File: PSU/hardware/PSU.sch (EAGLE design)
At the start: 202 parts, among them J1 SWD, J2 UART, Q1 PMOS-DPAK, Q10 PMOS-SOT23, Q11 NPN, Q2 PMOS-SOT23, Q3 NPN, Q4 PMOS-SOT23, Q5 NMOS-SOT23, Q6 PMOS-DPAK, Q7 PMOS-SOT23, Q8 NMOS-SOT23, Q9 PMOS-DPAK, U1 LM2576, U10 4069, U11 LTV-247, U12 74HC08, U13 STM8S003K3T6C, U14 74HC08, U15 4051, U16 358, U17 358, U18 74HC32, U2 MT3608, U3 7805, U4 324, U5 MC34063, U6 MT3608, U7 LM2576, U8 MC34063, U9 TP4056

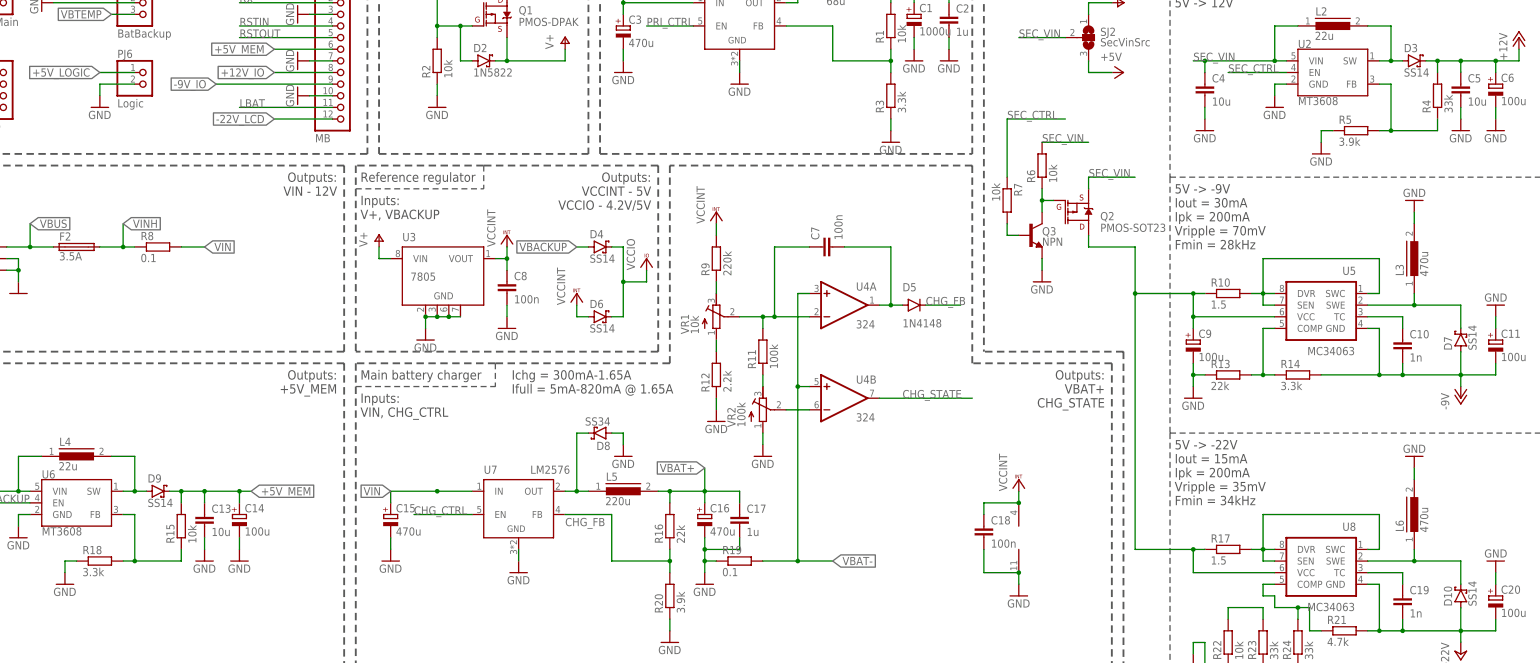
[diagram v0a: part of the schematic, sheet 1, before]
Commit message: [HW/PSU] Fix MT3608 feedback divider values
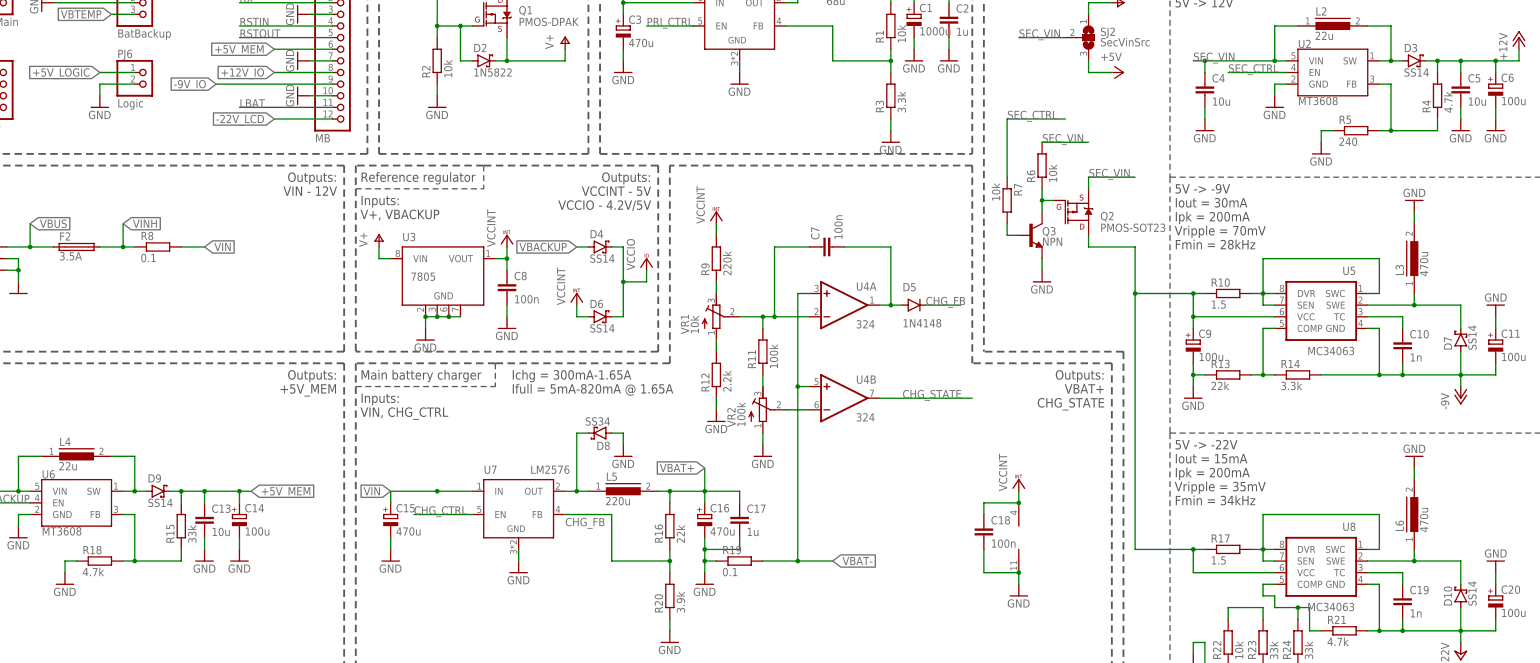
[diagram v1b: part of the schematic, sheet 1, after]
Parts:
- R15: value 10k -> 33k
- R18: value 3.3k -> 4.7k
- R4: value 33k -> 4.7k
- R5: value 3.9k -> 240
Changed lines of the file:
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@@
 </part>
 <part name="L3" library="custom" deviceset="COIL0608" device="" value="470u"/>
-<part name="R4" library="rcl" library_urn="urn:adsk.eagle:library:334" deviceset="R-EU_" device="R0805" package3d_urn="urn:adsk.eagle:package:23553/2" value="33k"/>
+<part name="R4" library="rcl" library_urn="urn:adsk.eagle:library:334" deviceset="R-EU_" device="R0805" package3d_urn="urn:adsk.eagle:package:23553/2" value="4.7k"/>
 <part name="C4" library="rcl" library_urn="urn:adsk.eagle:library:334" deviceset="C-EU" device="C1206" package3d_urn="urn:adsk.eagle:package:23618/2" value="10u"/>
 <part name="GND34" library="supply1" library_urn="urn:adsk.eagle:library:371" deviceset="GND" device=""/>
@@
 <part name="C5" library="rcl" library_urn="urn:adsk.eagle:library:334" deviceset="C-EU" device="C1206" package3d_urn="urn:adsk.eagle:package:23618/2" value="10u"/>
 <part name="GND36" library="supply1" library_urn="urn:adsk.eagle:library:371" deviceset="GND" device=""/>
-<part name="R5" library="rcl" library_urn="urn:adsk.eagle:library:334" deviceset="R-EU_" device="R0805" package3d_urn="urn:adsk.eagle:package:23553/2" value="3.9k"/>
+<part name="R5" library="rcl" library_urn="urn:adsk.eagle:library:334" deviceset="R-EU_" device="R0805" package3d_urn="urn:adsk.eagle:package:23553/2" value="240"/>
 <part name="GND37" library="supply1" library_urn="urn:adsk.eagle:library:371" deviceset="GND" device=""/>
 <part name="C6" library="rcl" library_urn="urn:adsk.eagle:library:334" deviceset="CPOL-EU" device="E3.5-8" package3d_urn="urn:adsk.eagle:package:23360/2" value="100u"/>
@@
 <part name="GND56" library="supply1" library_urn="urn:adsk.eagle:library:371" deviceset="GND" device=""/>
 <part name="U6" library="custom" deviceset="MT3608" device="" value="MT3608"/>
-<part name="R15" library="rcl" library_urn="urn:adsk.eagle:library:334" deviceset="R-EU_" device="R0805" package3d_urn="urn:adsk.eagle:package:23553/2" value="10k"/>
+<part name="R15" library="rcl" library_urn="urn:adsk.eagle:library:334" deviceset="R-EU_" device="R0805" package3d_urn="urn:adsk.eagle:package:23553/2" value="33k"/>
 <part name="C12" library="rcl" library_urn="urn:adsk.eagle:library:334" deviceset="C-EU" device="C1206" package3d_urn="urn:adsk.eagle:package:23618/2" value="10u"/>
 <part name="GND57" library="supply1" library_urn="urn:adsk.eagle:library:371" deviceset="GND" device=""/>
@@
 <part name="C13" library="rcl" library_urn="urn:adsk.eagle:library:334" deviceset="C-EU" device="C1206" package3d_urn="urn:adsk.eagle:package:23618/2" value="10u"/>
 <part name="GND59" library="supply1" library_urn="urn:adsk.eagle:library:371" deviceset="GND" device=""/>
-<part name="R18" library="rcl" library_urn="urn:adsk.eagle:library:334" deviceset="R-EU_" device="R0805" package3d_urn="urn:adsk.eagle:package:23553/2" value="3.3k"/>
+<part name="R18" library="rcl" library_urn="urn:adsk.eagle:library:334" deviceset="R-EU_" device="R0805" package3d_urn="urn:adsk.eagle:package:23553/2" value="4.7k"/>
 <part name="GND60" library="supply1" library_urn="urn:adsk.eagle:library:371" deviceset="GND" device=""/>
 <part name="C14" library="rcl" library_urn="urn:adsk.eagle:library:334" deviceset="CPOL-EU" device="E3.5-8" package3d_urn="urn:adsk.eagle:package:23360/2" value="100u"/>

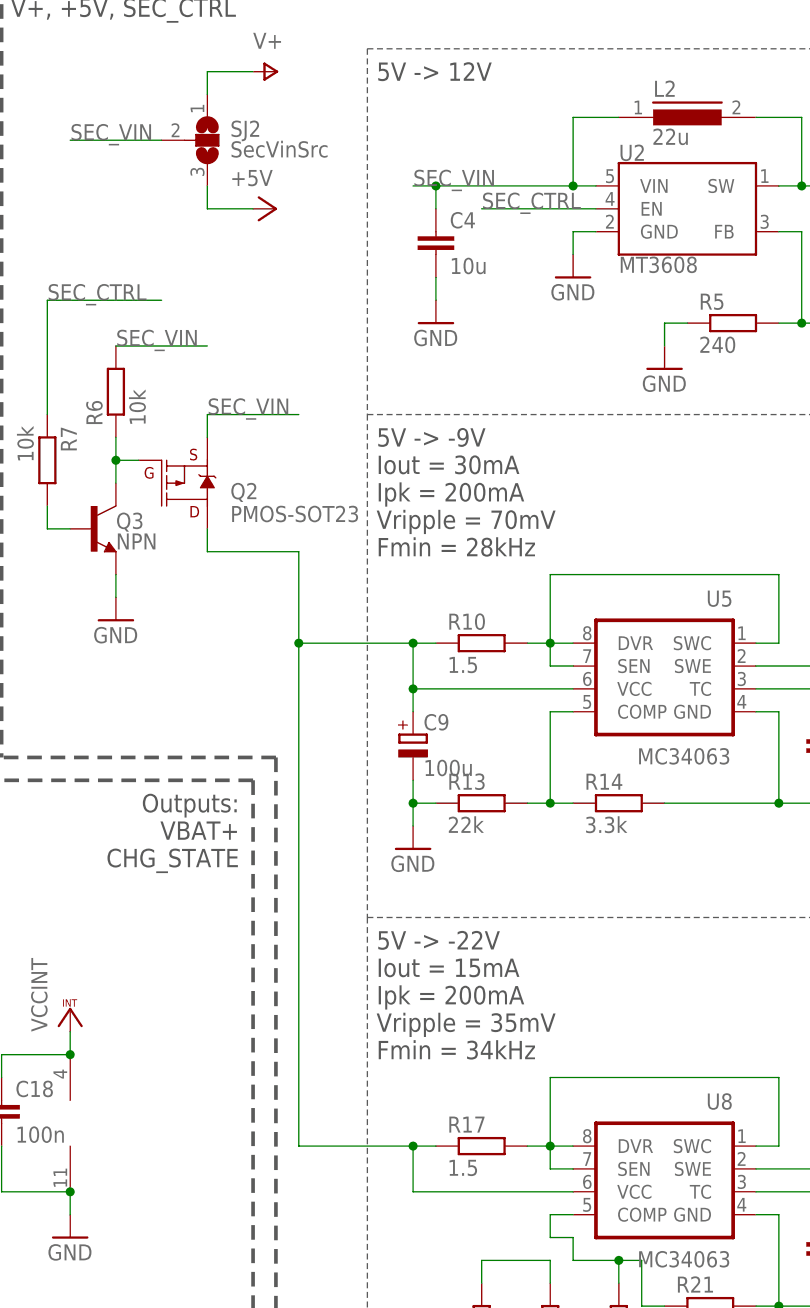
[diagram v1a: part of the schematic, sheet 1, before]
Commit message: [HW/PSU] Fix secondary 12V regulator enabling
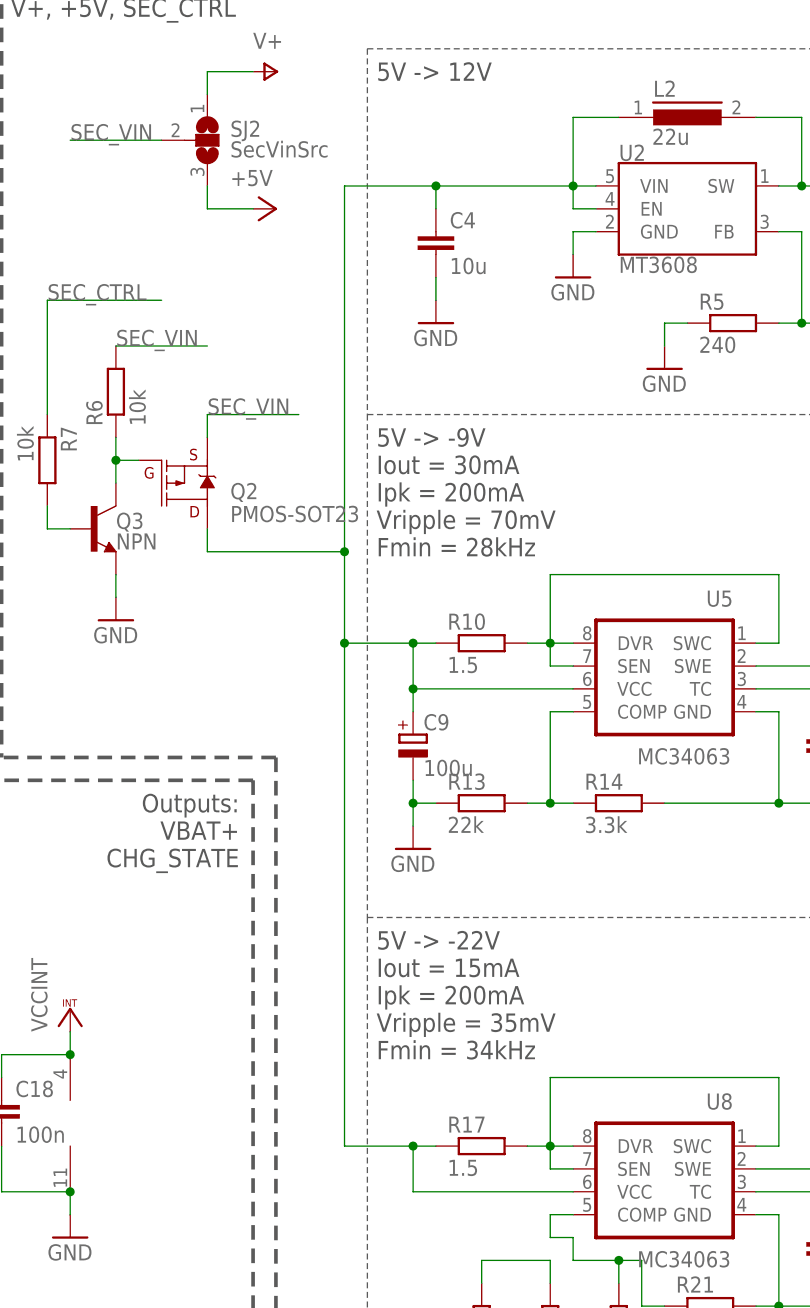
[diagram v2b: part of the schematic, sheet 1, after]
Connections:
- net SEC_CTRL: no longer U2.EN
- net SEC_VIN: no longer C4.1, L2.1, U2.VIN
- net SEC_VIN_SW: now also C4.1, L2.1, U2.EN, U2.VIN
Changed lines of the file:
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@@
-</segment>
-<segment>
-<pinref part="U2" gate="G$1" pin="VIN"/>
-<wire x1="325.12" y1="220.98" x2="322.58" y2="220.98" width="0.1524" layer="91"/>
-<pinref part="C4" gate="G$1" pin="1"/>
-<wire x1="322.58" y1="220.98" x2="307.34" y2="220.98" width="0.1524" layer="91"/>
-<wire x1="307.34" y1="220.98" x2="307.34" y2="218.44" width="0.1524" layer="91"/>
-<wire x1="327.66" y1="228.6" x2="322.58" y2="228.6" width="0.1524" layer="91"/>
-<wire x1="322.58" y1="228.6" x2="322.58" y2="220.98" width="0.1524" layer="91"/>
-<junction x="322.58" y="220.98"/>
-<wire x1="307.34" y1="220.98" x2="304.8" y2="220.98" width="0.1524" layer="91"/>
-<junction x="307.34" y="220.98"/>
-<label x="304.8" y="220.98" size="1.778" layer="95"/>
-<pinref part="L2" gate="G$1" pin="1"/>
 </segment>
 <segment>
@@
 </net>
 <net name="SEC_CTRL" class="1">
-<segment>
-<pinref part="U2" gate="G$1" pin="EN"/>
-<wire x1="325.12" y1="218.44" x2="312.42" y2="218.44" width="0.1524" layer="91"/>
-<label x="312.42" y="218.44" size="1.778" layer="95"/>
-</segment>
 <segment>
 <pinref part="R7" gate="G$1" pin="1"/>
@@
 <segment>
 <pinref part="U8" gate="G$1" pin="VCC"/>
-<wire x1="292.1" y1="180.34" x2="292.1" y2="170.18" width="0.1524" layer="91"/>
-<wire x1="292.1" y1="170.18" x2="292.1" y2="114.3" width="0.1524" layer="91"/>
+<wire x1="297.18" y1="180.34" x2="297.18" y2="170.18" width="0.1524" layer="91"/>
+<wire x1="297.18" y1="170.18" x2="297.18" y2="114.3" width="0.1524" layer="91"/>
 <wire x1="322.58" y1="109.22" x2="304.8" y2="109.22" width="0.1524" layer="91"/>
 <wire x1="304.8" y1="109.22" x2="304.8" y2="114.3" width="0.1524" layer="91"/>
 <pinref part="R17" gate="G$1" pin="1"/>
 <wire x1="307.34" y1="114.3" x2="304.8" y2="114.3" width="0.1524" layer="91"/>
-<wire x1="292.1" y1="114.3" x2="304.8" y2="114.3" width="0.1524" layer="91"/>
+<wire x1="297.18" y1="114.3" x2="304.8" y2="114.3" width="0.1524" layer="91"/>
 <junction x="304.8" y="114.3"/>
 <pinref part="Q2" gate="G$1" pin="D"/>
 <wire x1="281.94" y1="182.88" x2="281.94" y2="180.34" width="0.1524" layer="91"/>
-<wire x1="281.94" y1="180.34" x2="292.1" y2="180.34" width="0.1524" layer="91"/>
+<wire x1="281.94" y1="180.34" x2="297.18" y2="180.34" width="0.1524" layer="91"/>
 <pinref part="C9" gate="G$1" pin="+"/>
 <pinref part="R10" gate="G$1" pin="1"/>
@@
 <junction x="304.8" y="165.1"/>
 <wire x1="304.8" y1="165.1" x2="304.8" y2="162.56" width="0.1524" layer="91"/>
-<wire x1="304.8" y1="170.18" x2="292.1" y2="170.18" width="0.1524" layer="91"/>
-<junction x="292.1" y="170.18"/>
+<wire x1="304.8" y1="170.18" x2="297.18" y2="170.18" width="0.1524" layer="91"/>
+<junction x="297.18" y="170.18"/>
 <junction x="304.8" y="170.18"/>
+<junction x="297.18" y="180.34"/>
+<pinref part="U2" gate="G$1" pin="VIN"/>
+<wire x1="325.12" y1="220.98" x2="322.58" y2="220.98" width="0.1524" layer="91"/>
+<pinref part="C4" gate="G$1" pin="1"/>
+<wire x1="322.58" y1="220.98" x2="307.34" y2="220.98" width="0.1524" layer="91"/>
+<wire x1="307.34" y1="220.98" x2="307.34" y2="218.44" width="0.1524" layer="91"/>
+<wire x1="327.66" y1="228.6" x2="322.58" y2="228.6" width="0.1524" layer="91"/>
+<wire x1="322.58" y1="228.6" x2="322.58" y2="220.98" width="0.1524" layer="91"/>
+<junction x="322.58" y="220.98"/>
+<junction x="307.34" y="220.98"/>
+<pinref part="L2" gate="G$1" pin="1"/>
+<pinref part="U2" gate="G$1" pin="EN"/>
+<wire x1="325.12" y1="218.44" x2="322.58" y2="218.44" width="0.1524" layer="91"/>
+<wire x1="322.58" y1="218.44" x2="322.58" y2="220.98" width="0.1524" layer="91"/>
+<wire x1="297.18" y1="180.34" x2="297.18" y2="220.98" width="0.1524" layer="91"/>
+<wire x1="297.18" y1="220.98" x2="307.34" y2="220.98" width="0.1524" layer="91"/>
 </segment>
 </net>
